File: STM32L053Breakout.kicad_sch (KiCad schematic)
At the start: 59 parts, among them J1 USB_B_Micro, J2 Conn_Coaxial, J3 Male Pinheader 1x20, J4 Male Pinheader 1x20, J5 ARM 10pin, SW1 SW_Push, SW2 SW_Push, SW3 SW_Push, SW4 BOOT0_Switch, SW5 Reset_Switch, U1 RFM95W-868S2, U2 AMS1117-3.3, U3 L80-R, U4 STM32L053R8T6, Y1 Crystal_GND24

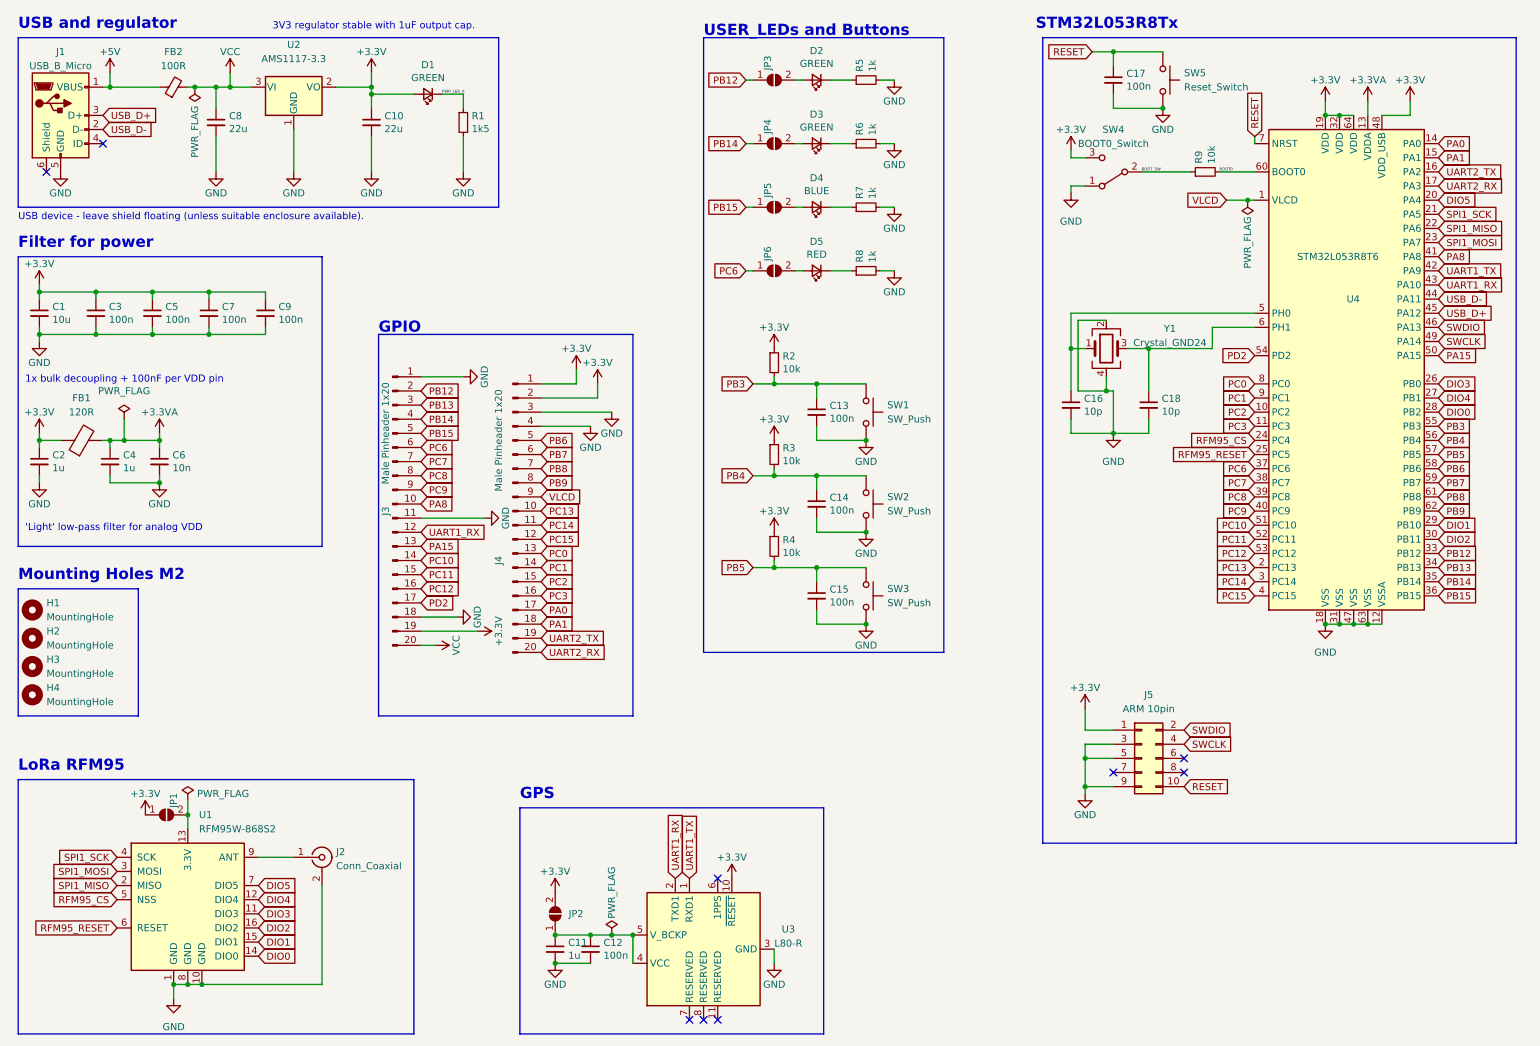
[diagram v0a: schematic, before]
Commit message: Add sensor and change bom for GPS
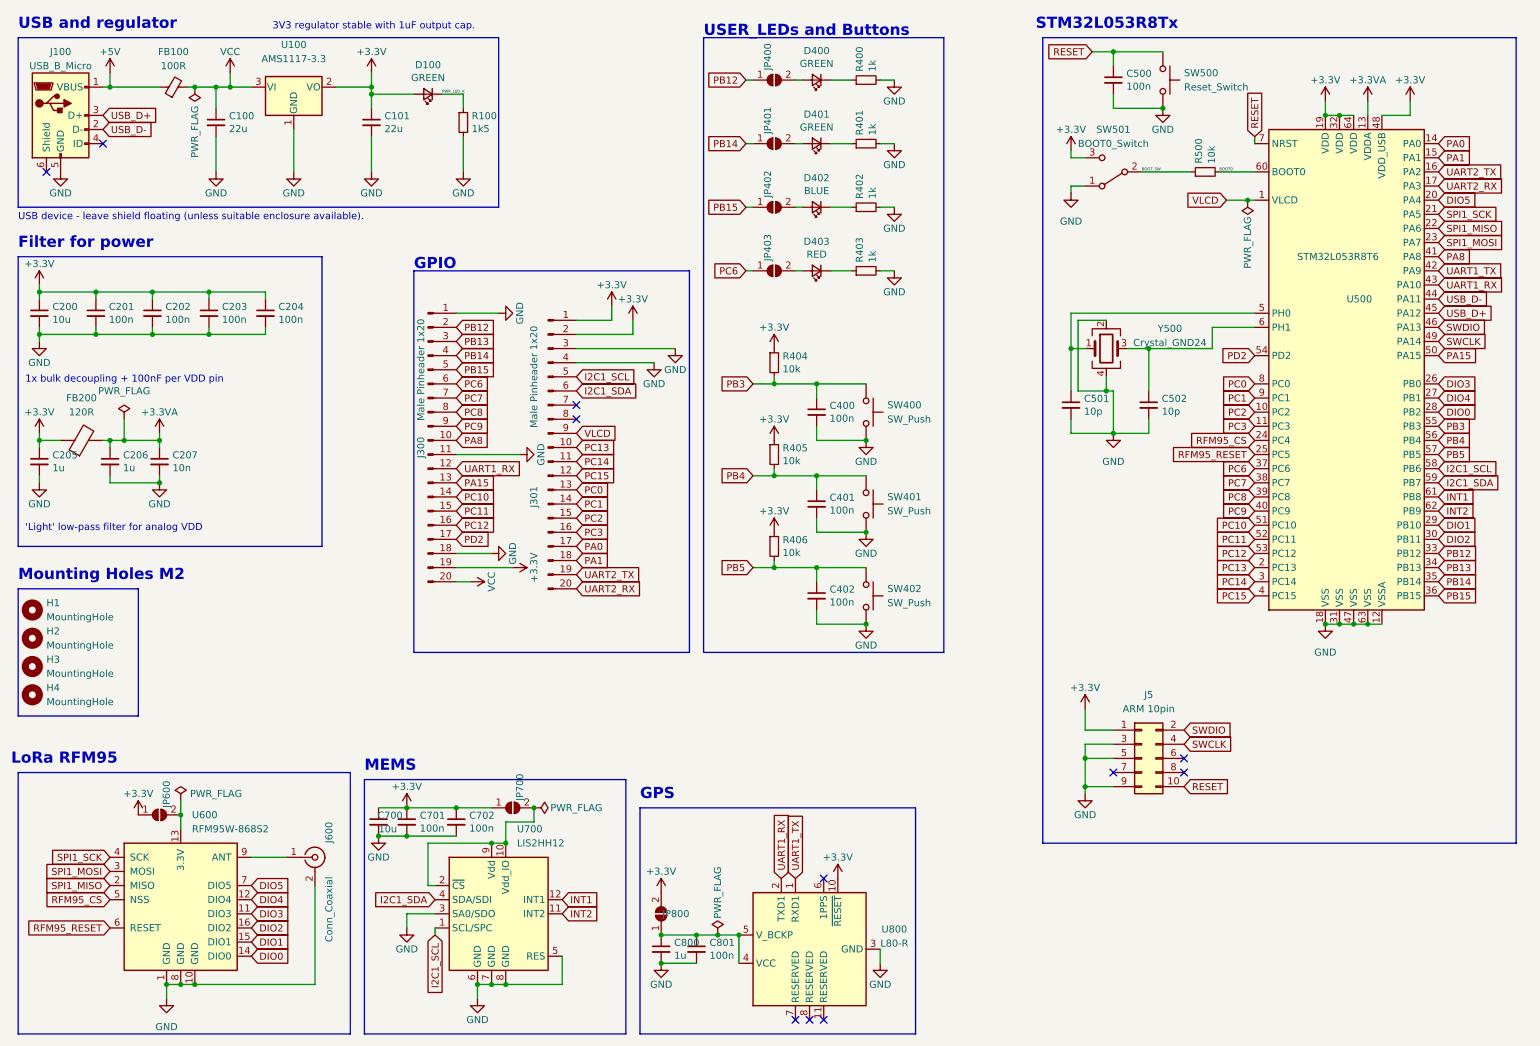
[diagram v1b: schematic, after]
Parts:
- added C700: 10u, Capacitor_SMD:C_0603_1608Metric, symbol Device:C_Small
- added C701, C702: 100n, Capacitor_SMD:C_0402_1005Metric, symbol Device:C_Small
- added JP700: SolderJumper_2_Open, Jumper:SolderJumper-2_P1.3mm_Open_Pad1.0x1.5mm, symbol Jumper:SolderJumper_2_Open
- added U700: LIS2HH12, Package_LGA:LGA-12_2x2mm_P0.5mm, symbol Sensor_Motion:LIS2HH12
- U800: renamed from U3; LCSC Part # C188357 -> C133488
- renumbered C8 to C100, C10 to C101, C1 to C200, C3 to C201, C5 to C202, C7 to C203, C9 to C204, C2 to C205, C4 to C206, C6 to C207, C13 to C400, C14 to C401, C15 to C402, C17 to C500, C16 to C501, C18 to C502, C11 to C800, C12 to C801, D1 to D100, D2 to D400, D3 to D401, D4 to D402, D5 to D403, FB2 to FB100, FB1 to FB200, J1 to J100, J3 to J300, J4 to J301, J2 to J600, JP3 to JP400, JP4 to JP401, JP5 to JP402, JP6 to JP403, JP1 to JP600, JP2 to JP800, R1 to R100, R5 to R400, R6 to R401, R7 to R402, R8 to R403, R2 to R404, R3 to R405, R4 to R406, R9 to R500, SW1 to SW400, SW2 to SW401, SW3 to SW402, SW5 to SW500, SW4 to SW501, U2 to U100, U4 to U500, U1 to U600, Y1 to Y500
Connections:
- net +3.3V: now also C700.1, C701.1, C702.1, JP700.1 (A)
- net GND: now also C700.2, C701.2, C702.2, U700.3 (SA0/SDO), U700.5 (RES), U700.6 (GND), U700.7 (GND), U700.8 (GND)
- net PB6 renamed I2C1_SCL
- net I2C1_SCL: now also U700.1 (SCL/SPC)
- net PB7 renamed I2C1_SDA
- net I2C1_SDA: now also U700.4 (SDA/SDI)
- net PB8: no longer names the net of J301.7 (Pin_7)
- net PB8: no longer U500.61 (PB8)
- net PB9: no longer names the net of J301.8 (Pin_8)
- net PB9: no longer U500.62 (PB9)
- new net: JP700.2 (B), U700.10 (Vdd_IO), U700.2 (~{CS}), U700.9 (Vdd)
- new net INT1: U500.61 (PB8), U700.12 (INT1)
- new net INT2: U500.62 (PB9), U700.11 (INT2)
- no-connect marks 9 -> 11
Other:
- note added: "MEMS"
- moved on the sheet: C800, C801, J300, J301, J600, JP600, JP800, U600, U800

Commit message: Change BOM for JLC
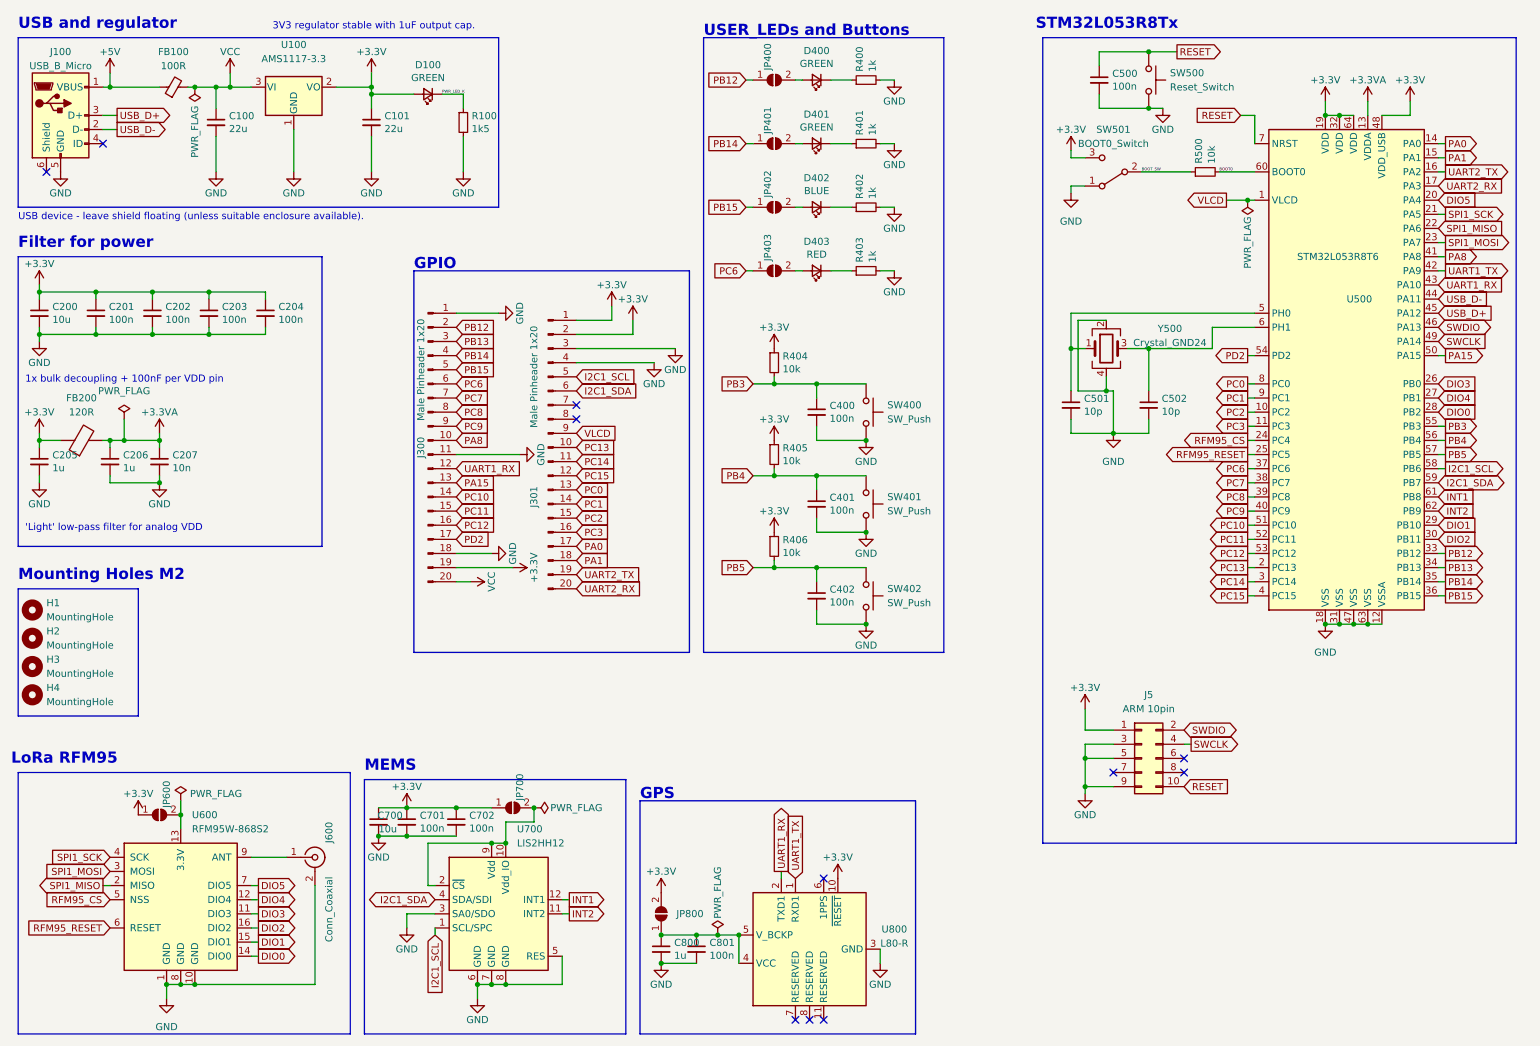
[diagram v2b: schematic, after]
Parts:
- C100, C101: LCSC Part # (none) -> C59461
- C200: LCSC Part # (none) -> C96446
- C201, C202, C203, C204, C400, C401, C402, C500, C801: LCSC Part # (none) -> C307331
- C205, C206, C800: LCSC Part # (none) -> C15849
- C207: LCSC Part # (none) -> C15195
- C501, C502: LCSC Part # (none) -> C32949
- C700: LCSC Part # C85713 -> C96446
- C701, C702: LCSC Part # C60474 -> C307331
- J5: LCSC Part # (none) -> C239059
- R100: LCSC Part # (none) -> C22843
- R400, R401, R402, R403: LCSC Part # (none) -> C21190
- R404, R405, R406, R500: LCSC Part # (none) -> C25804
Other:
- moved on the sheet: C500, SW500
